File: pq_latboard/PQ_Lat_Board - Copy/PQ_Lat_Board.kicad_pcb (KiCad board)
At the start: 6 copper layers, 48 x 48 mm, 27 parts, among them IC1 TCN75AVOA713, J1 Conn_01x11_MountingPin, J2 Conn_Coaxial

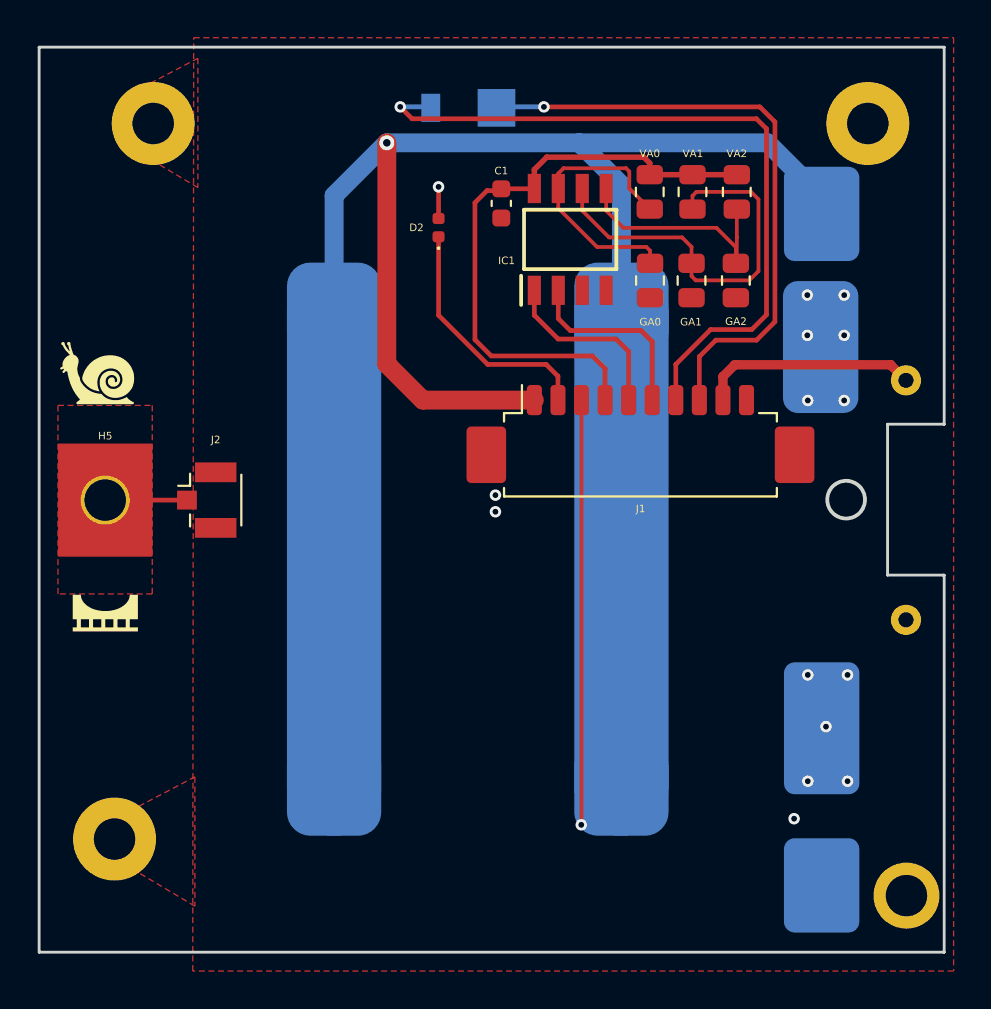
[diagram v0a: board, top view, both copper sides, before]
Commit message: lateral fixed
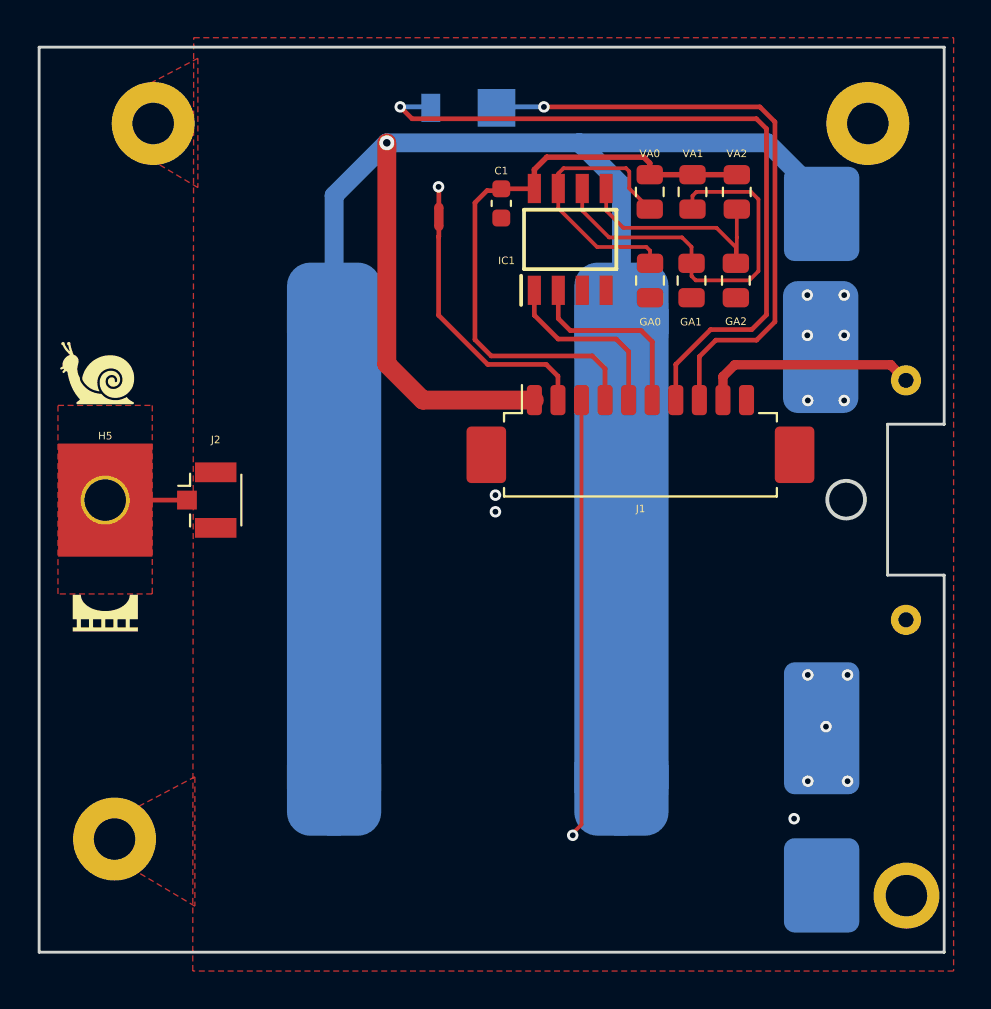
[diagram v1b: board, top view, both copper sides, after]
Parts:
- removed D2: LED, LED_SMD:LED_0402_1005Metric
- added NT1: NetTie_2, NetTie:NetTie-2_SMD_Pad0.5mm, F.Cu at (96.2, 51.0)
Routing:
- net /ADCS: track 13.1 -> 13.7 mm
